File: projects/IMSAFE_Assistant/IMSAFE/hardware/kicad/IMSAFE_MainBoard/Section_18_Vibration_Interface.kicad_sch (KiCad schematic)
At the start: 0 parts

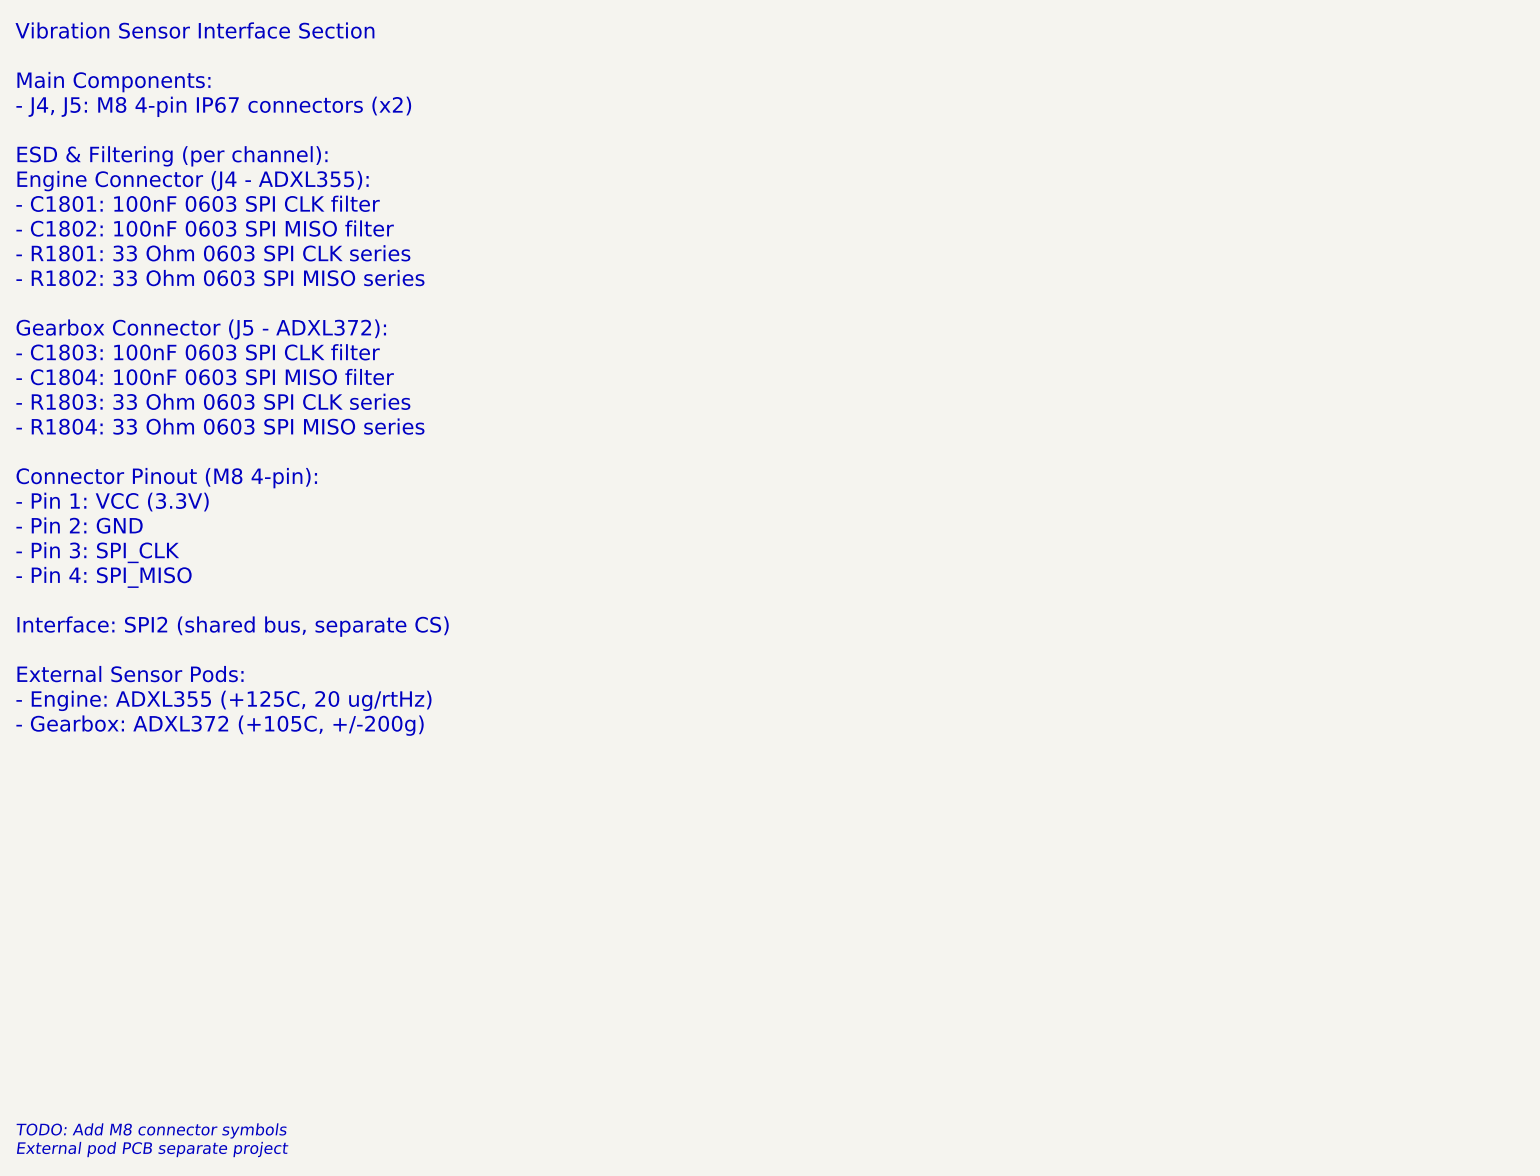
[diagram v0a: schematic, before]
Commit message: Add CAN-FD vibration sensor interface and remote pod design
- Update Section 18 schematic from SPI to CAN-FD interface
  - Add TCAN1042-Q1 transceiver with split termination
  - Configure FDCAN1 on PD0/PD1
  - Add ESD protection (PESD2CAN) and M8 4-pin connector
  - Remove on-board ADXL sensors (now on remote pods)

- Create IMSAFE_SensorPod KiCad project for remote vibration pods
  - STM32G0B1KET6 MCU with FDCAN support
  - AP2112K-3.3 LDO for 5V to 3.3V conversion
  - Support for ADXL355 (engine) and ADXL372 (gearbox) variants
  - Complete BOM and design notes

- Add vibration sensor documentation
  - Trade study for ADXL355 vs ADXL372 sensor selection
  - Connection strategy with CAN-FD architecture details
  - ADXL354/ADXL355 and ADXL372 datasheet summaries

Co-Authored-By: Claude Opus 4.5 <noreply@anthropic.com>
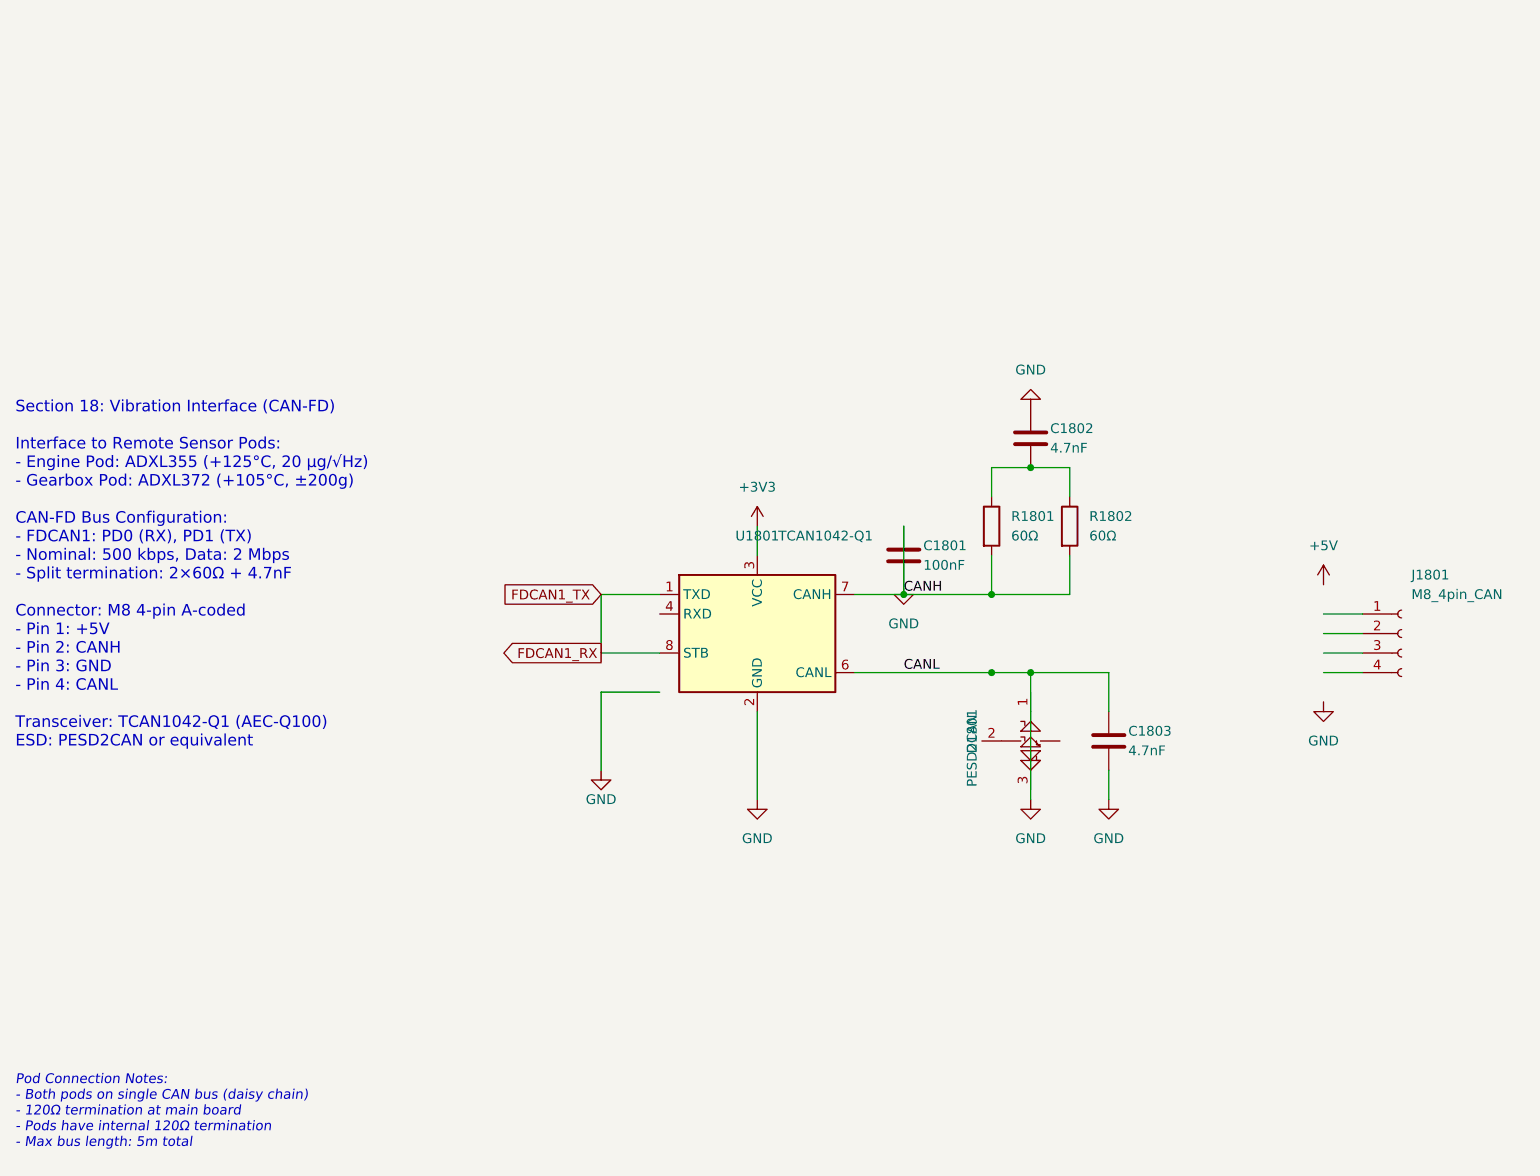
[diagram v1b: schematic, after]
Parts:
- added C1801: 100nF, Capacitor_SMD:C_0603_1608Metric, symbol Device:C
- added C1802, C1803: 4.7nF, Capacitor_SMD:C_0603_1608Metric, symbol Device:C
- added D1801: PESD2CAN, Package_TO_SOT_SMD:SOT-23, symbol Device:D_TVS_x2_AAC
- added J1801: M8_4pin_CAN, symbol Connector:Conn_01x04_Socket
- added R1801, R1802: 60Ω, Resistor_SMD:R_0603_1608Metric, symbol Device:R
- added U1801: TCAN1042-Q1, Package_SO:SOIC-8_3.9x4.9mm_P1.27mm, symbol Interface_CAN_LIN:TCAN1042
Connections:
- new net: C1802.2, R1801.1, R1802.1
- new net +3V3: U1801.3 (VCC)
- new net CANH: C1801.1, R1801.2, R1802.2, U1801.7 (CANH)
- new net FDCAN1_RX: U1801.1 (TXD), U1801.8 (STB)
- new net GND: C1801.2, C1802.1, C1803.1, C1803.2, U1801.2 (GND), U1801.6 (CANL)
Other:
- note added: "Pod Connection Notes: - Both pods on single CAN bus (daisy chain) - 120Ω termination at main board - Pods have internal 120Ω termination - Max bus length: 5m total"
- note added: "Section 18: Vibration Interface (CAN-FD) Interface to Remote Sensor Pods: - Engine Pod: ADXL355 (+125°C, 20 µg/√Hz) - Gearbox Pod: ADXL372 (+105°C, ±200g) CAN-FD Bus Configuration: - FDCAN1: PD0 (RX), PD1 (TX) - Nominal: 500 kbps, Data: 2 Mbps - Split termination: 2×60Ω + 4.7nF Connector: M8 4-pin A-coded - Pin 1: +5V - Pin 2: CANH - Pin 3: GND - Pin 4: CANL Transceiver: TCAN1042-Q1 (AEC-Q100) ES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"
- note removed: "TODO: Add M8 connector symbols External pod PCB separate project"
- note removed: "Vibration Sensor Interface Section Main Components: - J4, J5: M8 4-pin IP67 connectors (x2) ESD & Filtering (per channel): Engine Connector (J4 - ADXL355): - C1801: 100nF 0603 SPI CLK filter - C1802: 100nF 0603 SPI MISO filter - R1801: 33 Ohm 0603 SPI CLK series - R1802: 33 Ohm 0603 SPI MISO series Gearbox Connector (J5 - ADXL372): - C1803: 100nF 0603 SPI CLK filter - C1804: 100nF 0603 SPI MISO f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"
- title: Section 18: Vibration Sensor Interface -> Section 18: Vibration Interface
